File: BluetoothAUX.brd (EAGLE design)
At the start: 38.7 x 28.6 mm, 17 parts, among them IC2 TPA6132A2, X1 STEREOJACK, X2 MINI-USB-SCHIELD-32005-201

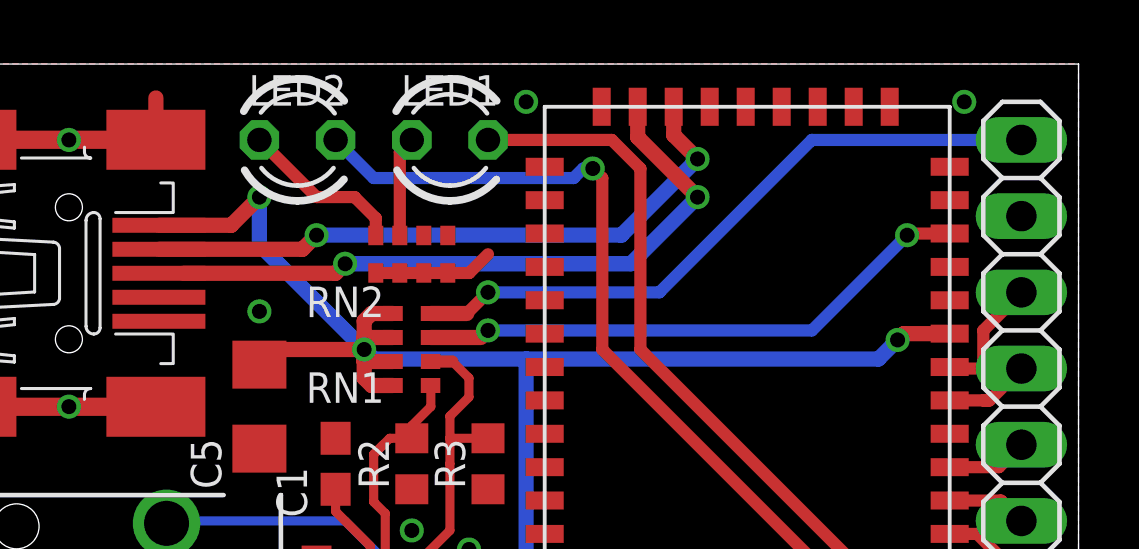
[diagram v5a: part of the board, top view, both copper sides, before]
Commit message: Remove unused COM pin
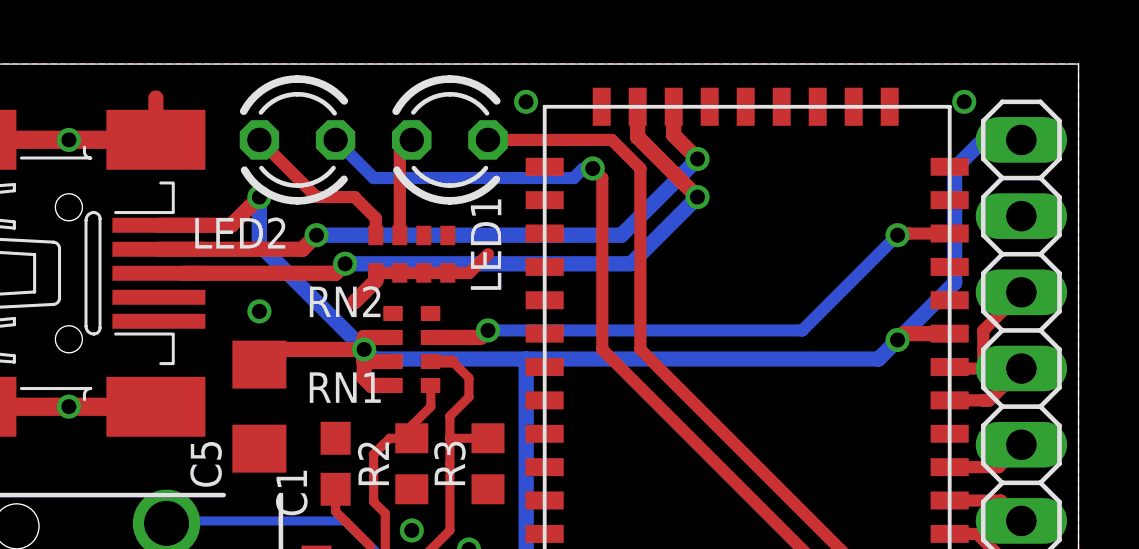
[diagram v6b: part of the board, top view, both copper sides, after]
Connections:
- removed net COM: JP10.1, RN1.4
- net +5V: now also JP10.1; no longer RN1.5
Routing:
- net COM: track 22.1 -> 0.00 mm, vias 1 -> 0
- net +5V: track 64.1 -> 70.4 mm
- net GND: track 23.9 -> 25.2 mm
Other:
- board text added: "+5V"
- board text removed: "COM"
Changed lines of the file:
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@@
 <setting verticaltext="up"/>
 </settings>
-<grid distance="0.05" unitdist="inch" unit="inch" style="lines" multiple="1" display="yes" altdistance="0.0125" altunitdist="inch" altunit="inch"/>
+<grid distance="0.05" unitdist="inch" unit="mm" style="lines" multiple="1" display="yes" altdistance="0.0125" altunitdist="inch" altunit="inch"/>
 <layers>
 <layer number="1" name="Top" color="4" fill="1" visible="yes" active="yes"/>
@@
 <layer number="24" name="bOrigins" color="15" fill="1" visible="yes" active="yes"/>
 <layer number="25" name="tNames" color="7" fill="1" visible="yes" active="yes"/>
-<layer number="26" name="bNames" color="7" fill="1" visible="no" active="yes"/>
+<layer number="26" name="bNames" color="7" fill="1" visible="yes" active="yes"/>
 <layer number="27" name="tValues" color="7" fill="1" visible="no" active="yes"/>
 <layer number="28" name="bValues" color="7" fill="1" visible="no" active="yes"/>
@@
 <layer number="49" name="Reference" color="7" fill="1" visible="yes" active="yes"/>
 <layer number="50" name="dxf" color="7" fill="1" visible="no" active="no"/>
-<layer number="51" name="tDocu" color="7" fill="1" visible="yes" active="yes"/>
-<layer number="52" name="bDocu" color="7" fill="1" visible="yes" active="yes"/>
+<layer number="51" name="tDocu" color="7" fill="1" visible="no" active="yes"/>
+<layer number="52" name="bDocu" color="7" fill="1" visible="no" active="yes"/>
 <layer number="53" name="tGND_GNDA" color="7" fill="9" visible="no" active="no"/>
 <layer number="54" name="bGND_GNDA" color="1" fill="9" visible="no" active="no"/>
@@
 <text x="81.28" y="26.035" size="1.016" layer="22" font="vector" rot="MR180" align="center-right">CS</text>
 <text x="81.28" y="23.495" size="1.016" layer="22" font="vector" rot="MR180" align="center-right">MISO</text>
-<text x="81.28" y="41.275" size="1.016" layer="22" font="vector" rot="MR180" align="center-right">COM</text>
+<text x="81.28" y="41.275" size="1.016" layer="22" font="vector" rot="MR180" align="center-right">+5V</text>
 <rectangle x1="66.675" y1="15.24" x2="80.3275" y2="21.59" layer="41"/>
 <rectangle x1="66.675" y1="15.24" x2="80.3275" y2="21.59" layer="42"/>
@@
 </element>
 <element name="LED2" library="led" library_urn="urn:adsk.eagle:library:259" package="LED3MM" package3d_urn="urn:adsk.eagle:package:15797/1" value="" x="58.42" y="41.275" smashed="yes">
-<attribute name="NAME" x="58.42" y="42.926" size="1.016" layer="25" font="vector" ratio="10" align="center"/>
+<attribute name="NAME" x="56.515" y="38.1635" size="1.016" layer="25" font="vector" ratio="10" align="center"/>
 <attribute name="VALUE" x="60.325" y="39.624" size="1.27" layer="27" ratio="10"/>
 </element>
 <element name="LED1" library="led" library_urn="urn:adsk.eagle:library:259" package="LED3MM" package3d_urn="urn:adsk.eagle:package:15797/1" value="" x="63.5" y="41.275" smashed="yes">
-<attribute name="NAME" x="63.5" y="42.926" size="1.016" layer="25" font="vector" ratio="10" align="center"/>
+<attribute name="NAME" x="64.7065" y="37.7825" size="1.016" layer="25" font="vector" ratio="10" rot="R90" align="center"/>
 <attribute name="VALUE" x="65.405" y="39.624" size="1.27" layer="27" ratio="10"/>
 </element>
@@
 <wire x1="66.675" y1="21.59" x2="66.66" y2="21.575" width="0.6096" layer="1"/>
 <contactref element="R2" pad="1"/>
-<contactref element="R3" pad="1"/>
 <contactref element="C1" pad="2"/>
 <contactref element="C2" pad="2"/>
@@
 <contactref element="RN2" pad="3"/>
 <contactref element="RN2" pad="4"/>
-<wire x1="61.03" y1="36.84" x2="63.43" y2="36.84" width="0.4064" layer="1"/>
+<wire x1="63.43" y1="36.84" x2="61.03" y2="36.84" width="0.4064" layer="1"/>
 <via x="57.15" y="35.56" extent="1-16" drill="0.5"/>
 <wire x1="63.43" y1="36.84" x2="64.145" y2="36.84" width="0.4064" layer="1"/>
 <wire x1="64.145" y1="36.84" x2="64.77" y2="37.465" width="0.4064" layer="1"/>
+<contactref element="R3" pad="1"/>
+<wire x1="61.03" y1="36.84" x2="61.03" y2="36.5825" width="0.508" layer="1"/>
+<wire x1="61.03" y1="36.5825" x2="60.325" y2="35.8775" width="0.508" layer="1"/>
 </signal>
 <signal name="+5V" class="1">
@@
 <contactref element="IC2" pad="14"/>
 <contactref element="R1" pad="2"/>
-<wire x1="60.6425" y1="34.29" x2="60.6425" y2="34.69" width="0.508" layer="1"/>
-<wire x1="60.6425" y1="34.29" x2="60.6425" y2="33.89" width="0.508" layer="1"/>
 <wire x1="61.345" y1="22.02" x2="61.345" y2="20.8875" width="0.3048" layer="1"/>
 <wire x1="53.8" y1="38.43" x2="56.21" y2="38.43" width="0.508" layer="1"/>
@@
 <wire x1="57.15" y1="37.7825" x2="60.6425" y2="34.29" width="0.508" layer="16"/>
 <via x="60.6425" y="34.29" extent="1-16" drill="0.5"/>
-<wire x1="80.16" y1="34.8175" x2="78.6325" y2="34.8175" width="0.508" layer="1"/>
+<wire x1="78.6325" y1="34.8175" x2="80.16" y2="34.8175" width="0.508" layer="1"/>
 <wire x1="78.6325" y1="34.8175" x2="78.4225" y2="34.6075" width="0.508" layer="1"/>
 <via x="78.4225" y="34.6075" extent="1-16" drill="0.5"/>
@@
 <wire x1="64.77" y1="18.63" x2="64.77" y2="19.3675" width="0.3048" layer="1"/>
 <wire x1="64.77" y1="19.3675" x2="65.0875" y2="19.685" width="0.3048" layer="1"/>
-<wire x1="60.6425" y1="34.29" x2="60.6425" y2="35.2425" width="0.508" layer="1"/>
-<wire x1="60.89" y1="35.49" x2="60.6425" y2="35.2425" width="0.508" layer="1"/>
 <wire x1="60.6425" y1="33.3375" x2="60.6425" y2="34.29" width="0.508" layer="1"/>
 <wire x1="60.89" y1="33.09" x2="60.6425" y2="33.3375" width="0.508" layer="1"/>
@@
 <contactref element="RN1" pad="7"/>
 <contactref element="RN1" pad="6"/>
-<contactref element="RN1" pad="5"/>
 <wire x1="61.605" y1="33.09" x2="60.89" y2="33.09" width="0.508" layer="1"/>
 <wire x1="61.605" y1="33.89" x2="60.6425" y2="33.89" width="0.508" layer="1"/>
@@
 <wire x1="61.605" y1="34.69" x2="60.6425" y2="34.69" width="0.508" layer="1"/>
 <wire x1="60.6425" y1="34.69" x2="60.6425" y2="34.29" width="0.508" layer="1"/>
-<wire x1="61.605" y1="35.49" x2="60.89" y2="35.49" width="0.508" layer="1"/>
+<contactref element="JP10" pad="1"/>
+<wire x1="78.4225" y1="34.6075" x2="80.3275" y2="36.5125" width="0.508" layer="16"/>
+<wire x1="80.3275" y1="36.5125" x2="80.3275" y2="40.3225" width="0.508" layer="16"/>
+<wire x1="80.3275" y1="40.3225" x2="81.28" y2="41.275" width="0.508" layer="16"/>
+<wire x1="81.28" y1="41.275" x2="82.55" y2="41.275" width="0.508" layer="16"/>
 </signal>
 <signal name="VBUS_1.8V">
@@
 <wire x1="80.065" y1="38.155" x2="80.16" y2="38.155" width="0.4064" layer="1"/>
 <wire x1="80.16" y1="38.155" x2="78.795" y2="38.155" width="0.4064" layer="1"/>
-<wire x1="78.795" y1="38.155" x2="78.74" y2="38.1" width="0.4064" layer="1"/>
-<via x="78.74" y="38.1" extent="1-16" drill="0.5"/>
+<wire x1="78.795" y1="38.155" x2="78.4225" y2="38.1" width="0.4064" layer="1"/>
+<via x="78.4225" y="38.1" extent="1-16" drill="0.5"/>
 <via x="64.77" y="34.925" extent="1-16" drill="0.5"/>
 <wire x1="64.77" y1="34.925" x2="64.535" y2="34.69" width="0.4064" layer="1"/>
-<wire x1="64.77" y1="34.925" x2="75.565" y2="34.925" width="0.4064" layer="16"/>
-<wire x1="75.565" y1="34.925" x2="78.74" y2="38.1" width="0.4064" layer="16"/>
+<wire x1="64.77" y1="34.925" x2="75.2475" y2="34.925" width="0.4064" layer="16"/>
+<wire x1="75.2475" y1="34.925" x2="78.4225" y2="38.1" width="0.4064" layer="16"/>
 <contactref element="RN1" pad="3"/>
 <wire x1="64.535" y1="34.69" x2="62.855" y2="34.69" width="0.508" layer="1"/>
 </signal>
-<signal name="COM">
-<contactref element="JP10" pad="1"/>
-<wire x1="82.55" y1="41.275" x2="75.565" y2="41.275" width="0.4064" layer="16"/>
-<wire x1="75.565" y1="41.275" x2="70.485" y2="36.195" width="0.4064" layer="16"/>
-<wire x1="70.485" y1="36.195" x2="64.77" y2="36.195" width="0.4064" layer="16"/>
-<via x="64.77" y="36.195" extent="1-16" drill="0.5"/>
-<wire x1="64.77" y1="36.195" x2="64.065" y2="35.49" width="0.4064" layer="1"/>
-<contactref element="RN1" pad="4"/>
-<wire x1="64.065" y1="35.49" x2="62.855" y2="35.49" width="0.508" layer="1"/>
-</signal>
 <signal name="BAT">

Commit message: Make smaller
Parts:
- removed LED2: (no value), led:LED3MM
- removed R1: 10K, resistor:R0603
- removed X1: STEREOJACK, adafruit:STX3100
- removed X2: MINI-USB-SCHIELD-32005-201, con-cypressindustries:32005-201
- added J3: AUDIO_JACK_TRRSSMD_RA, SparkFun-Connectors:AUDIO_JACK_3.5MM_TRRS_SMD_RA
- added J4: USB, SparkFun-Connectors:USB-MICROB
- LED1: value (none) -> RGBLED5050; device led:LED3MM -> adafruit:RGBLED5050
- R2, R3: value (none) -> 0
- RN2: value 1K -> 220
- U$1: device BT:F3188 -> BluetoothAUX:F3188
- moved RN2 29.1 mm to (88.3, 24.4), turned to 90 degrees
- moved LED1 26.4 mm to (83.8, 24.4), turned to 180 degrees
- moved C5 26.4 mm to (81.6, 42.2), turned to 0 degrees
- moved R3 24.8 mm to (89.5, 32.1)
- moved C2 24.3 mm to (81.3, 28.9)
- moved IC2 23.9 mm to (83.2, 33.7)
- moved C4 22.1 mm to (83.8, 28.9)
- moved R2 21.5 mm to (81.9, 39.1), turned to 270 degrees
- moved C1 20.6 mm to (79.7, 35.6), turned to 180 degrees
- moved C3 19.8 mm to (78.7, 28.9)
- moved RN1 16.3 mm to (77.8, 39.1)
- moved U$1 10.2 mm to (83.8, 30.5), flipped to the bottom
- moved JP10 7.62 mm to (74.9, 32.4), flipped to the bottom
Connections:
- net N$26 renamed CPP
- net N$27 renamed CPN
- net N$28 renamed HPVSS
- net N$29 renamed HVPDD
- net N$31 renamed G0
- net N$32 renamed G1
- removed net LED1+: LED1.K, U$1.P$3
- removed net LED1-: LED1.A, RN2.7
- removed net LED2+: LED2.K, U$1.P$2
- removed net LED2-: LED2.A, RN2.8
- removed net N$13: RN1.3, U$1.P$15
- removed net N$14: IC2.5, X1.2
- removed net N$18: U$1.P$24, X2.2
- removed net N$19: U$1.P$25, X2.3
- removed net N$20: IC2.16, X1.5
- removed net N$30: IC2.13, R1.1
- new net LED0: LED1.4, U$1.P$3
- new net LED1: LED1.5, U$1.P$2
- new net LED2: LED1.6, U$1.P$1
- new net LED_B: LED1.3, RN2.5
- new net LED_G: LED1.1, RN2.8
- new net LED_R: LED1.2, RN2.7
- new net OUTL: IC2.16, J3.TIP
- new net OUTR: IC2.5, J3.RING1
- new net POWER_EN: RN1.4, U$1.P$15
- new net TPA_EN: IC2.13, RN1.3
- new net USB_N: J4.D-, U$1.P$24
- new net USB_P: J4.D+, U$1.P$25
- net +5V: now also J4.VBUS, RN1.5; no longer R1.2, X2.1
- net GND: now also J4.GND, J4.MT1, J4.MT2, J4.P$1, J4.P$2; no longer X2.5, X2.M1, X2.M2, X2.M3, X2.M4
- net SGND: now also J3.EARTH; no longer X1.1
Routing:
- net +5V: track 70.4 -> 36.0 mm, vias 4 -> 3
- net LED2+: track 31.4 -> 0.00 mm, vias 1 -> 0
- net LED1+: track 25.7 -> 0.00 mm
- net N$19: track 22.8 -> 0.00 mm, vias 2 -> 0
- net N$18: track 21.3 -> 0.00 mm, vias 2 -> 0
- net GND: track 25.2 -> 4.30 mm, vias 16 -> 18
- net USB_P: track 0.00 -> 19.5 mm, vias 0 -> 1
- net N$13: track 18.8 -> 0.00 mm, vias 2 -> 0
- net USB_N: track 0.00 -> 16.1 mm, vias 0 -> 1
- net TPA_EN: track 0.00 -> 15.7 mm, vias 0 -> 2
- net N$20: track 13.4 -> 0.00 mm, vias 1 -> 0
- net OUTL: track 0.00 -> 13.3 mm, vias 0 -> 2
- net SGND: track 24.8 -> 12.2 mm, vias 1 -> 2
- net OUTR: track 0.00 -> 11.9 mm, vias 0 -> 2
- net SPK_LP: track 3.78 -> 15.0 mm, vias 0 -> 1
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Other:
- board size 38.7 x 28.6 mm -> 19.7 x 27.9 mm
